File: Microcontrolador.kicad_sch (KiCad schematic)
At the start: 1 part, among them IC2 R7F125FPL4AFB-C#UA0

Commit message: He corregido los errores de la tarea 2 y he añadido los condensadores de desacople.
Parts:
- removed IC2: R7F125FPL4AFB-C#UA0, QFP50P1600X1600X160-100N, symbol R7F125FPL4AFB-C#UA0:R7F125FPL4AFB-C#UA0
- added C1, C2, C3, C4(desacople)1: 100n, Capacitor_SMD:C_0805_2012Metric, symbol Device:C
- added J2: Conn_01x06_Pin, Connector_PinHeader_2.54mm:PinHeader_1x06_P2.54mm_Horizontal, symbol Connector:Conn_01x06_Pin
- added R1, R2, R3: 10k, Resistor_SMD:R_0805_2012Metric, symbol Device:R
- added U1: STM32G030K8Tx, Package_QFP:LQFP-32_7x7mm_P0.8mm, symbol MCU_ST_STM32G0:STM32G030K8Tx
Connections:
- net GND: now also C1.2, C2.2, C3.2, C4(desacople)1.2, J2.2 (Pin_2), U1.5 (VSS)
- net VDD: now also C4(desacople)1.1, J2.1 (Pin_1), U1.4 (VDD)
- new net: C3.1, R3.1, U1.7 (PA0)
- new net: C2.1, R2.1, U1.8 (PA1)
- new net: J2.6 (Pin_6), R2.2
- new net: C1.1, R1.1, U1.9 (PA2)
- new net: J2.5 (Pin_5), R3.2
- new net: J2.3 (Pin_3), U1.24 (PA13)
- new net: J2.4 (Pin_4), U1.25 (PA14)

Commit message: he actualizado el jumper con uno de 7 pines en vez de 6 porque R1 estaba sin conectar
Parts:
- removed J2: Conn_01x06_Pin, Connector_PinHeader_2.54mm:PinHeader_1x06_P2.54mm_Horizontal, symbol Connector:Conn_01x06_Pin
- added J3: Conn_01x07, Connector_PinHeader_2.54mm:PinHeader_1x07_P2.54mm_Horizontal, symbol Connector_Generic:Conn_01x07
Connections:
- net GND: now also J3.2 (Pin_2)
- net VDD: now also J3.1 (Pin_1)
- net at R2.2: now also J3.6 (Pin_6)
- net at R1.2: now also J3.7 (Pin_7)
- net at R3.2: now also J3.5 (Pin_5)
- net at U1.24 (PA13): now also J3.3 (Pin_3)
- net at U1.25 (PA14): now also J3.4 (Pin_4)
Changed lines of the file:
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@@
+	(wire
+		(pts
+			(xy 186.69 64.77) (xy 186.69 60.96)
+		)
+		(stroke
+			(width 0)
+			(type default)
+		)
+	)
 	(wire
 		(pts
@@
 	(wire
 		(pts
-			(xy 186.69 60.96) (xy 186.69 64.77)
-		)
-		(stroke
-			(width 0)
-			(type default)
-		)
-	)
-	(wire
-		(pts
 			(xy 204.47 67.31) (xy 170.18 67.31)
 		)
@@
 	(wire
 		(pts
+			(xy 165.1 69.85) (xy 204.47 69.85)
+		)
+		(stroke
+			(width 0)
+			(type default)
+		)
+	)
+	(wire
+		(pts
 			(xy 157.48 63.5) (xy 157.48 71.12)
 		)
@@
 	(wire
 		(pts
+			(xy 165.1 66.04) (xy 165.1 69.85)
+		)
+		(stroke
+			(width 0)
+			(type default)
+		)
+	)
+	(wire
+		(pts
+			(xy 204.47 64.77) (xy 186.69 64.77)
+		)
+		(stroke
+			(width 0)
+			(type default)
+		)
+	)
+	(wire
+		(pts
 			(xy 204.47 54.61) (xy 196.85 54.61)
 		)
@@
 	(wire
 		(pts
-			(xy 204.47 64.77) (xy 186.69 64.77)
+			(xy 152.4 66.04) (xy 165.1 66.04)
 		)
 		(stroke
@@
 	)
 	(symbol
+		(lib_id "Connector_Generic:Conn_01x07")
+		(at 209.55 62.23 0)
+		(unit 1)
+		(body_style 1)
+		(exclude_from_sim no)
+		(in_bom yes)
+		(on_board yes)
+		(in_pos_files yes)
+		(dnp no)
+		(fields_autoplaced yes)
+		(property "Reference" "J3"
+			(at 212.09 60.9599 0)
+			(show_name no)
+			(do_not_autoplace no)
+			(effects
+				(font
+					(size 1.27 1.27)
+				)
+				(justify left)
+			)
+		)
+		(property "Value" "Conn_01x07"
+			(at 212.09 63.4999 0)
+			(show_name no)
+			(do_not_autoplace no)
+			(effects
+				(font
+					(size 1.27 1.27)
+				)
+				(justify left)
+			)
+		)
+		(property "Footprint" "Connector_PinHeader_2.54mm:PinHeader_1x07_P2.54mm_Horizontal"
+			(at 209.55 62.23 0)
+			(hide yes)
+			(show_name no)
+			(do_not_autoplace no)
+			(effects
+				(font
+					(size 1.27 1.27)
+				)
+			)
+		)
+		(property "Datasheet" ""
+			(at 209.55 62.23 0)
+			(hide yes)
+			(show_name no)
+			(do_not_autoplace no)
+			(effects
+				(font
+					(size 1.27 1.27)
+				)
+			)
+		)
+		(property "Description" "Generic connector, single row, 01x07, script generated (kicad-library-utils/schlib/autogen/connector/)"
+			(at 209.55 62.23 0)
+			(hide yes)
+			(show_name no)
+			(do_not_autoplace no)
+			(effects
+				(font
+					(size 1.27 1.27)
+				)
+			)
+		)
+		(pin "1"
+		)
+		(pin "3"
+		)
+		(pin "5"
+		)
+		(pin "7"
+		)
+		(pin "4"
+		)
+		(pin "6"
+		)
+		(pin "2"
+		)
+		(instances
+			(project "tarea2"
+				(path "/2450fa96-bfdf-43ef-9d5c-9c389bfd976a/c8564780-9aca-4b31-b1dc-c1de95b47103"
+					(reference "J3")
+					(unit 1)
+				)
+			)
+		)
+	)
+	(symbol
 		(lib_id "MCU_ST_STM32G0:STM32G030K8Tx")
 		(at 114.3 81.28 0)
@@
 					(unit 1)
 				)
-			)
-		)
-	)
-	(symbol
-		(lib_id "Connector:Conn_01x06_Pin")
-		(at 209.55 59.69 0)
-		(mirror y)
-		(unit 1)
-		(body_style 1)
-		(exclude_from_sim no)
-		(in_bom yes)
-		(on_board yes)
-		(in_pos_files yes)
-		(dnp no)
-		(property "Reference" "J2"
-			(at 208.915 49.53 0)
-			(show_name no)
-			(do_not_autoplace no)
-			(effects
-				(font
-					(size 1.27 1.27)
-				)
-			)
-		)
-		(property "Value" "Conn_01x06_Pin"
-			(at 208.915 52.07 0)
-			(hide yes)
-			(show_name no)
-			(do_not_autoplace no)
-			(effects
-				(font
-					(size 1.27 1.27)
-				)
-			)
-		)
-		(property "Footprint" "Connector_PinHeader_2.54mm:PinHeader_1x06_P2.54mm_Horizontal"
-			(at 209.55 59.69 0)
-			(hide yes)
-			(show_name no)
-			(do_not_autoplace no)
-			(effects
-				(font
-					(size 1.27 1.27)
-				)
-			)
-		)
-		(property "Datasheet" ""
-			(at 209.55 59.69 0)
-			(hide yes)
-			(show_name no)
-			(do_not_autoplace no)
-			(effects
-				(font
-					(size 1.27 1.27)
-				)
-			)
-		)
-		(property "Description" "Generic connector, single row, 01x06, script generated"
-			(at 209.55 59.69 0)
-			(hide yes)
-			(show_name no)
-			(do_not_autoplace no)
-			(effects
-				(font
-					(size 1.27 1.27)
-				)
-			)
-		)
-		(pin "1"
-		)
-		(pin "3"
-		)
-		(pin "5"
-		)
-		(pin "2"
-		)
-		(pin "6"
-		)
-		(pin "4"
-		)
-		(instances
-			(project "tarea2"
-				(path "/2450fa96-bfdf-43ef-9d5c-9c389bfd976a/c8564780-9aca-4b31-b1dc-c1de95b47103"
-					(reference "J2")
-					(unit 1)
-				)

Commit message: he marcado los pines sin conexión con una etiqueta de sin conexión para que no de error en ERC
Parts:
- added J2: BUS I2C, Connector_PinHeader_2.54mm:PinHeader_1x04_P2.54mm_Vertical, symbol Connector_Generic:Conn_01x04
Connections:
- net GND: now also J2.4 (Pin_4)
- net VDD: now also J2.3 (Pin_3)
- net at U1.30 (PB6): now also J2.1 (Pin_1)
- net at U1.31 (PB7): now also J2.2 (Pin_2)
- no-connect marks 0 -> 21

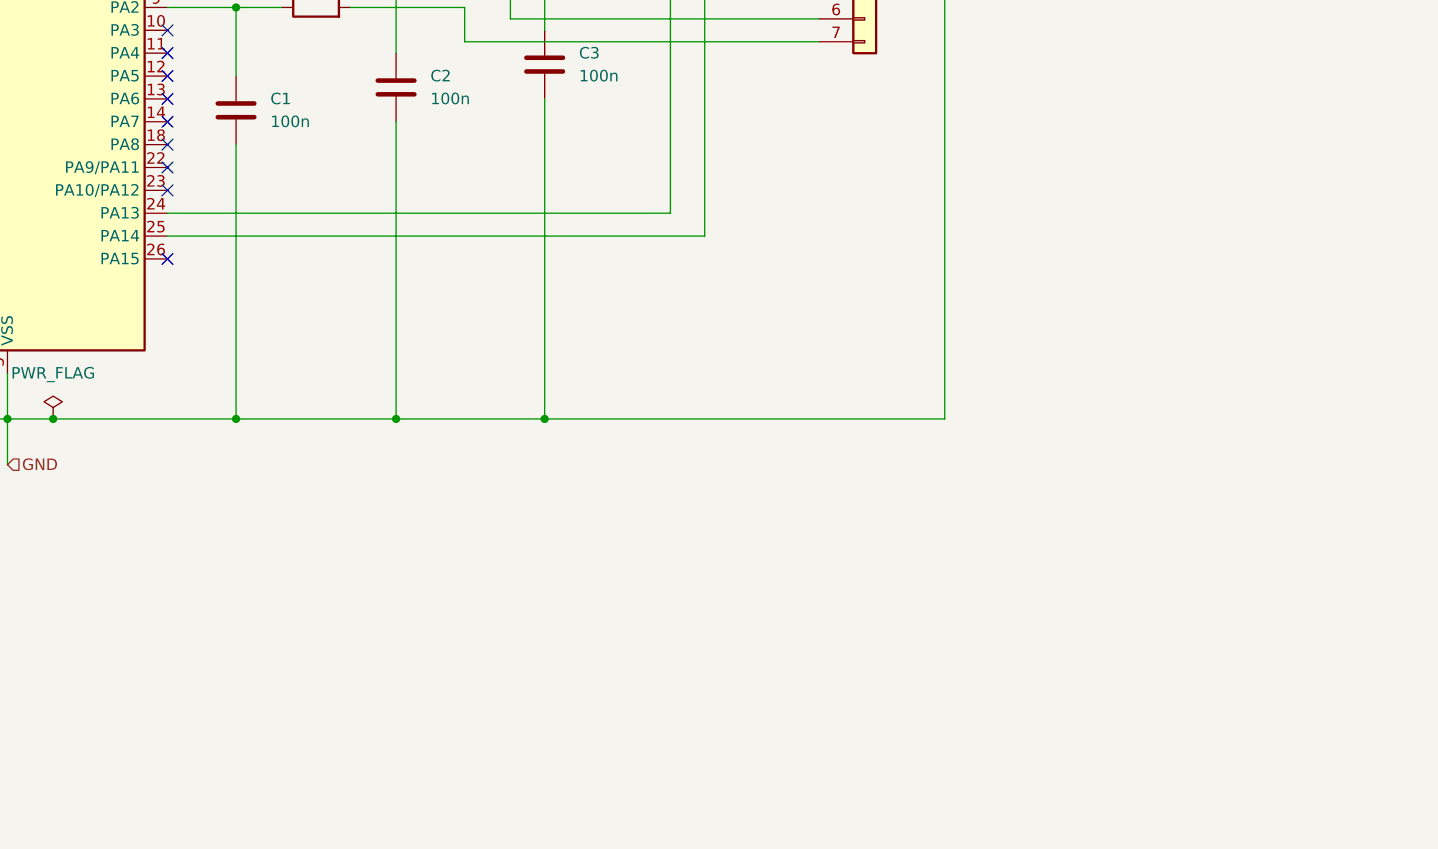
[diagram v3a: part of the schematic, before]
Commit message: Se han añadido un receptor de USB tipo C, un CH340 y sus respectivos componentes para su correcto funcionamiento para completar la tarea de enrutado diferencial de la Sesion-4
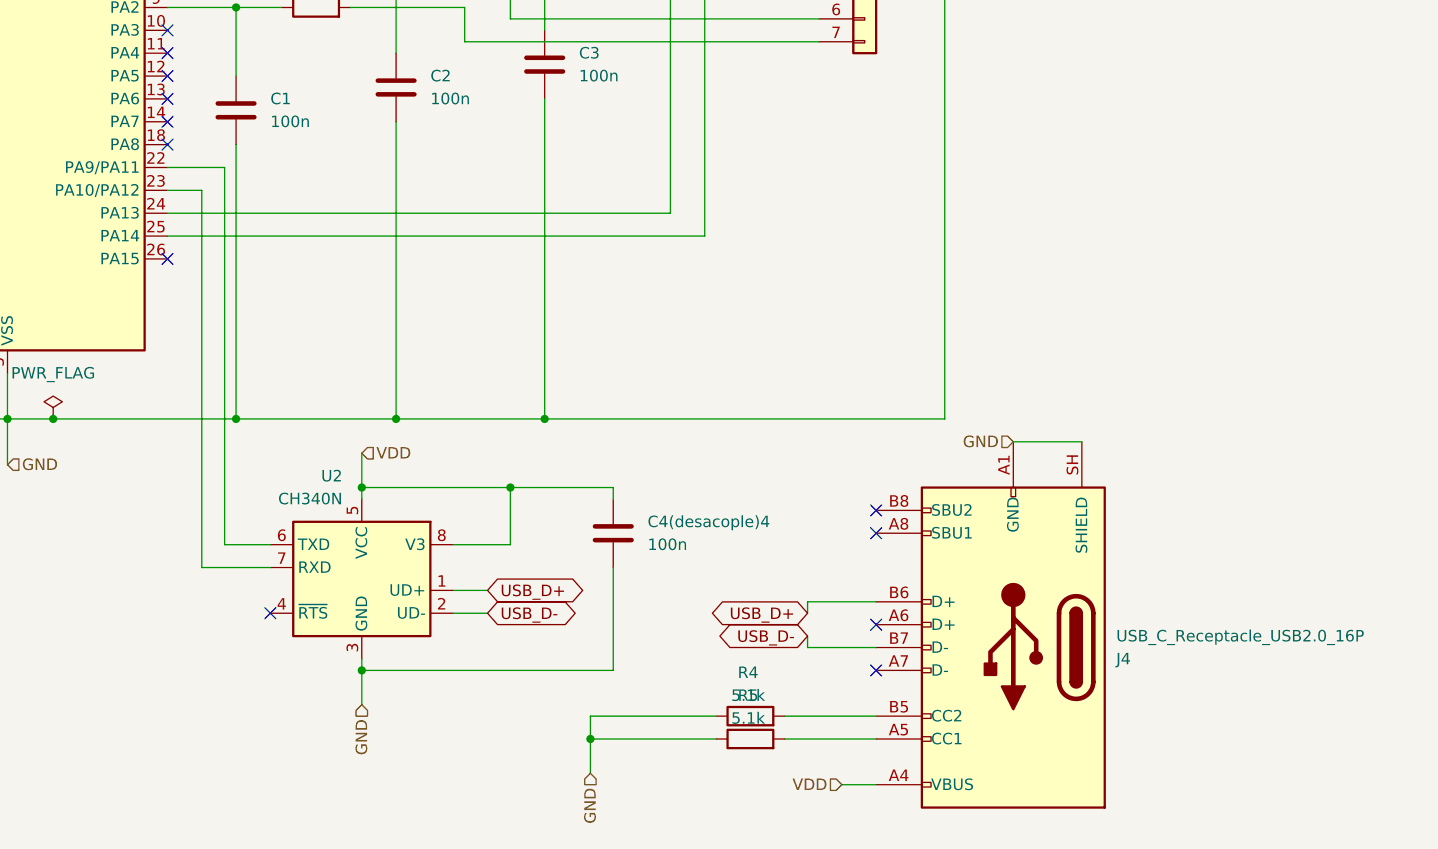
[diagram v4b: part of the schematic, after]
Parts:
- added C4(desacople)4: 100n, Capacitor_SMD:C_0805_2012Metric, symbol Device:C
- added J4: USB_C_Receptacle_USB2.0_16P, Connector_USB:USB_C_Receptacle_GCT_USB4105-xx-A_16P_TopMnt_Horizontal, symbol Connector:USB_C_Receptacle_USB2.0_16P
- added R4, R5: 5.1k, Resistor_SMD:R_0805_2012Metric, symbol Device:R
- added U2: CH340N, Package_SO:JEITA_SOIC-8_3.9x4.9mm_P1.27mm, symbol Interface_USB:CH340N
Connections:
- net GND: now also C4(desacople)4.2, J4.A1 (GND), J4.A12 (GND), J4.B1 (GND), J4.B12 (GND), J4.SH (SHIELD), R4.1, R5.1, U2.3 (GND)
- net VDD: now also C4(desacople)4.1, J4.A4 (VBUS), J4.A9 (VBUS), J4.B4 (VBUS), J4.B9 (VBUS), U2.5 (VCC), U2.8 (V3)
- net at U1.22 (PA9/PA11): now also U2.6 (TXD)
- net at U1.23 (PA10/PA12): now also U2.7 (RXD)
- new net: J4.A5 (CC1), R5.2
- new net: J4.B5 (CC2), R4.2
- new net USB_D+: J4.B6 (D+), U2.1 (UD+)
- new net USB_D-: J4.B7 (D-), U2.2 (UD-)
- no-connect marks 21 -> 24
